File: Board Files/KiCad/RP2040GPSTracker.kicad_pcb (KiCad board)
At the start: 2 copper layers, 99.6 x 53 mm, 116 parts, among them J1 BOOTSEL, J10 GNSS, J2 RESET, J3 DEBUG, J4 BT(LE), J5 GSM, J6 USBC_CHARGE, J7 USBC_PROG, J8 2822541-1, J9 BATTERY, U1 W25Q128JVS, U10 LM66200DRLR, U2 SIM868, U3 RP2040, U4 SN74LVC1G66DRYR, U5 LM66200DRLR, U6 MP2624GL, U7 NCP1117LPST33T3G, U8 SAFFB1G56KB0F5F, Y1 Crystal

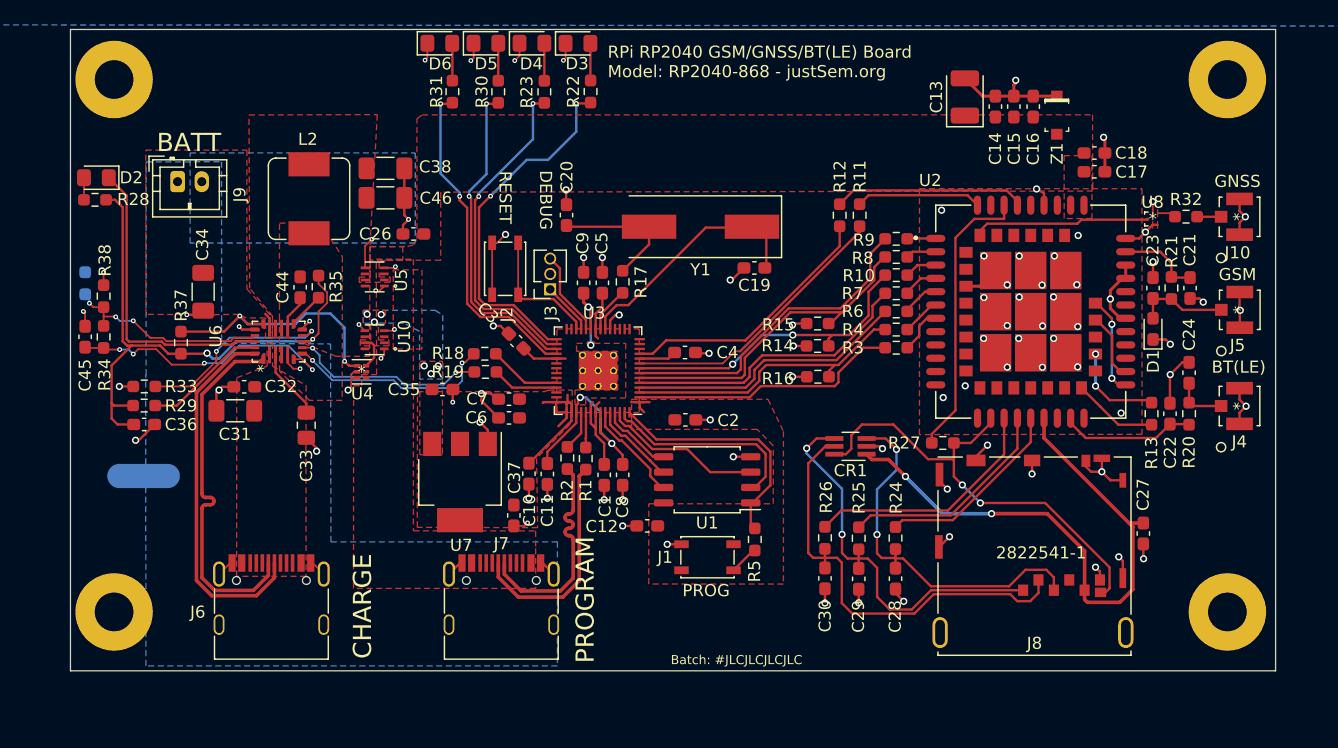
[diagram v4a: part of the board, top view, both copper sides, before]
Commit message: Rev 1.3. Implemented USB-C CC Channels. Fixed Z1 rotation. Expanded GPIO
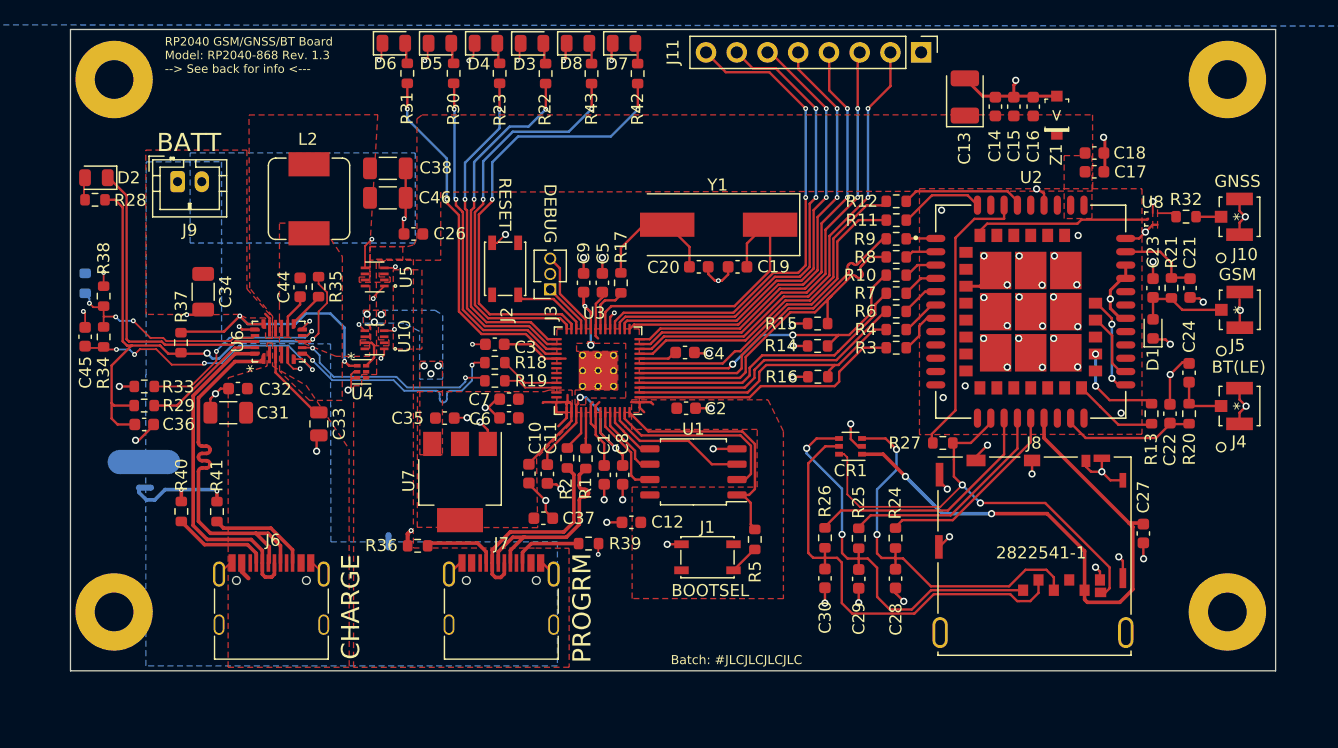
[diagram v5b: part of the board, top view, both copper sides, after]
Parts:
- removed REF**: Symbol_CC-Noncommercial_SilkscreenTop_Small, Symbol:Symbol_CC-Noncommercial_SilkscreenTop_Small
- removed REF**: Symbol_CC-Attribution_SilkscreenTop_Small, Symbol:Symbol_CC-Attribution_SilkscreenTop_Small
- removed REF**: Symbol_CC-ShareAlike_SilkscreenTop_Small, Symbol:Symbol_CC-ShareAlike_SilkscreenTop_Small
- removed REF**: Symbol_CreativeCommons_SilkscreenTop_Type2_Small, Symbol:Symbol_CreativeCommons_SilkscreenTop_Type2_Small
- added D7: LED, LED_SMD:LED_0805_2012Metric, F.Cu at (117.1, 5.01)
- added D8: LED, LED_SMD:LED_0805_2012Metric, F.Cu at (113.3, 5.01)
- added J11: GPIO9-15, Connector_PinHeader_2.54mm:PinHeader_1x08_P2.54mm_Vertical, F.Cu at (141.7, 5.76)
- added NT2: NetTie_2, NetTie:NetTie-2_SMD_Pad0.5mm, B.Cu at (77.6, 41.7)
- added NT3: NetTie_2, NetTie:NetTie-2_SMD_Pad0.5mm, B.Cu at (97.7, 46.2)
- added R36: 5.6k, Resistor_SMD:R_0603_1608Metric, F.Cu at (100.1, 46.5)
- added R39: 5.6k, Resistor_SMD:R_0603_1608Metric, F.Cu at (114.2, 46.3)
- added R40: 5.6k, Resistor_SMD:R_0603_1608Metric, F.Cu at (80.6, 43.7)
- added R41: 5.6k, Resistor_SMD:R_0603_1608Metric, F.Cu at (83.5, 43.7)
- added R42: 330, Resistor_SMD:R_0603_1608Metric, F.Cu at (118.3, 7.51)
- added R43: 330, Resistor_SMD:R_0603_1608Metric, F.Cu at (114.5, 7.51)
- C1, C10, C11, C12, C14, C15, C16, C17, C18, C19, C2, C20, C21, C22, C23, C24, C26, C27, C3, C32, C35, C36, C37, C4, C44, C45, C5, C6, C7, C8, C9: footprint Capacitor_SMD:C_0603_1608Metric_Pad1.08x0.95mm_HandSolder -> Capacitor_SMD:C_0603_1608Metric
- C28, C29, C30: value 100nF -> 22pF; footprint Capacitor_SMD:C_0603_1608Metric_Pad1.08x0.95mm_HandSolder -> Capacitor_SMD:C_0603_1608Metric
- C31, C34, C38, C46: footprint Capacitor_SMD:C_1206_3216Metric_Pad1.33x1.80mm_HandSolder -> Capacitor_SMD:C_1206_3216Metric
- C33: footprint Capacitor_SMD:C_0805_2012Metric_Pad1.18x1.45mm_HandSolder -> Capacitor_SMD:C_0805_2012Metric
- CR1: footprint Package_TO_SOT_SMD:SOT-363_SC-70-6_Handsoldering -> Package_TO_SOT_SMD:SOT-363_SC-70-6
- D1: footprint Diode_SMD:D_0603_1608Metric_Pad1.05x0.95mm_HandSolder -> Diode_SMD:D_0603_1608Metric
- D2, D3, D4, D5, D6: footprint LED_SMD:LED_0805_2012Metric_Pad1.15x1.40mm_HandSolder -> LED_SMD:LED_0805_2012Metric
- R1, R10, R11, R12, R13, R14, R15, R16, R17, R18, R19, R2, R20, R21, R22, R23, R24, R25, R26, R27, R28, R29, R3, R30, R31, R32, R33, R34, R35, R37, R38, R4, R5, R6, R7, R8, R9, TH1: footprint Resistor_SMD:R_0603_1608Metric_Pad0.98x0.95mm_HandSolder -> Resistor_SMD:R_0603_1608Metric
- moved C20 11.7 mm to (123.3, 23.5), turned to 0 degrees
- moved R12 4.81 mm to (139.6, 18.1), turned to 180 degrees
- moved R31 4.02 mm to (99.2, 7.49)
- moved R22 4.00 mm to (110.7, 7.51)
- moved R23 4.00 mm to (106.9, 7.49)
- moved R30 3.99 mm to (103.1, 7.49)
- moved D3 3.80 mm to (109.5, 5.01)
- moved D4 3.80 mm to (105.7, 5.00)
- moved D5 3.80 mm to (101.9, 5.00)
- moved D6 3.80 mm to (98.1, 5.00)
- moved R11 3.06 mm to (139.6, 19.6), turned to 180 degrees
- moved C37 2.45 mm to (110.5, 44.3), turned to 180 degrees
- moved C35 2.37 mm to (102.3, 36.0)
- moved C3 1.79 mm to (106.5, 29.9), turned to 0 degrees
- moved Y1 1.51 mm to (125.0, 20.0)
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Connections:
- J6 pad A5: unconnected-(J6-PadA5) -> Net-(J6-PadA5)
- J6 pad B5: unconnected-(J6-PadB5) -> Net-(J6-PadB5)
- J6 pad B6: unconnected-(J6-PadB6) -> /BCM_D+
- J6 pad B7: unconnected-(J6-PadB7) -> /BCM_D-
- J7 pad A5: unconnected-(J7-PadA5) -> Net-(J7-PadA5)
- J7 pad B5: unconnected-(J7-PadB5) -> Net-(J7-PadB5)
- J7 pad B6: unconnected-(J7-PadB6) -> /USB_D+
- J7 pad B7: unconnected-(J7-PadB7) -> /USB_D-
- U2 pad 41: (no net) -> unconnected-(U2-Pad41)
- U3 pad 12: unconnected-(U3-Pad12) -> /IO_1
- U3 pad 13: unconnected-(U3-Pad13) -> /IO_2
- U3 pad 14: unconnected-(U3-Pad14) -> /IO_3
- U3 pad 15: unconnected-(U3-Pad15) -> /IO_4
- U3 pad 16: unconnected-(U3-Pad16) -> /IO_5
- U3 pad 17: unconnected-(U3-Pad17) -> /IO_6
- U3 pad 18: unconnected-(U3-Pad18) -> /IO_7
- U3 pad 27: unconnected-(U3-Pad27) -> Net-(U3-Pad27)
- U3 pad 28: unconnected-(U3-Pad28) -> Net-(U3-Pad28)
- Z1 pad A: /SIM_PWR -> GND
- Z1 pad K: GND -> /SIM_PWR
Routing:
- net /IO_7: track 0.00 -> 41.4 mm, vias 0 -> 2
- net /IO_6: track 0.00 -> 39.9 mm, vias 0 -> 2
- net /IO_1: track 0.00 -> 38.7 mm, vias 0 -> 2
- net /IO_5: track 0.00 -> 38.4 mm, vias 0 -> 2
- net /IO_4: track 0.00 -> 37.6 mm, vias 0 -> 2
- net /IO_2: track 0.00 -> 37.2 mm, vias 0 -> 2
- net /IO_3: track 0.00 -> 37.0 mm, vias 0 -> 2
- net Net-(U3-Pad27): track 0.00 -> 36.9 mm, vias 0 -> 2
- net Net-(U3-Pad28): track 0.00 -> 33.6 mm, vias 0 -> 2
- net GND: track 125.2 -> 137.1 mm, vias 88 -> 92
- net Net-(J6-PadB5): track 0.00 -> 8.30 mm
- net Net-(J6-PadA5): track 0.00 -> 8.08 mm
- net Net-(J7-PadA5): track 0.00 -> 6.16 mm
- net Net-(J7-PadB5): track 0.00 -> 5.72 mm
- net /SIM_PWRKEY: track 15.9 -> 10.2 mm
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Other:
- board text added: "10"
- board text added: "11"
- board text added: "12"
- board text added: "13"
- board text added: "14"
- board text added: "15"
- board text added: "16"
- board text added: "17"
- board text added: "18"
- board text added: "19"
- board text added: "20"
- board text added: "21"
- board text added: "9"
- board text added: ">"
- board text added: "BOOTSEL"
- board text added: "Board Rev.: 1.3 18-03-2022"
- board text added: "GND"
- board text added: "GPIO#:"
- board text added: "Get started at wiki.justsem.org/rp2040-868"
- board text added: "LED D3"
- board text added: "LED D4"
- board text added: "LED D5"
- board text added: "LED D6"
- board text added: "LED D7"
- board text added: "LED D8"
- board text added: "PROGRM"
- board text added: "RP2040 GSM/GNSS/BT Board Model: RP2040-868 Rev. 1.3 --> See back for info <---"
- board text removed: "Board Rev.: 1.2 16-03-2022"
- board text removed: "Get started at docs.justsem.org/rp2040-868"
- board text removed: "PROG"
- board text removed: "PROGRAM"
- board text removed: "RPi RP2040 GSM/GNSS/BT(LE) Board Model: RP2040-868 - justSem.org"

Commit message: Rev 2.0
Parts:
- added ?: , RP2040-868Graphics:charge-fs, F.Cu at (94.4, 55.5)
- added ?: , RP2040-868Graphics:bt-re, F.Cu at (166.2, 32.0)
- added ?: , RP2040-868Graphics:gnss-re, F.Cu at (165.2, 16.3)
- added ?: , RP2040-868Graphics:program-fs, F.Cu at (113.6, 56.2)
- added ?: , RP2040-868Graphics:batt-ca, F.Cu at (81.6, 18.1)
- added ?: , RP2040-868Graphics:debug-ha, F.Cu at (114.3, 12.0)
- added ?: , RP2040-868Graphics:r2_0-ca, B.Cu at (136.1, 53.4)
- added ?: , RP2040-868Graphics:date-cc-ha, B.Cu at (141.9, 55.1)
- added ?: , RP2040-868Graphics:rev-cc-ha, B.Cu at (141.9, 53.4)
- added ?: , RP2040-868Graphics:9-ca, B.Cu at (139.2, 9.81)
- added ?: , RP2040-868Graphics:14-ca, B.Cu at (126.4, 10.5)
- added ?: , RP2040-868Graphics:status-lc-ha-left, F.Cu at (75.4, 14.7)
- added ?: , RP2040-868Graphics:12-ca, B.Cu at (131.5, 10.5)
- added ?: , RP2040-868Graphics:wikiref-re, B.Cu at (126.7, 28.2)
- added ?: , RP2040-868Graphics:15-ca, B.Cu at (123.9, 10.4)
- added ?: , RP2040-868Graphics:3v3-lc-ca, B.Cu at (121.4, 11.8)
- added ?: , RP2040-868Graphics:gnd-ca, B.Cu at (141.7, 12.1)
- added ?: , RP2040-868Graphics:13-ca, B.Cu at (129.0, 10.5)
- added ?: , RP2040-868Graphics:11-ca, B.Cu at (134.1, 10.3)
- added ?: , RP2040-868Graphics:10-ca, B.Cu at (136.6, 10.5)
- added ?: , RP2040-868Graphics:status-lc-ha, F.Cu at (82.2, 4.99)
- added ?: , RP2040-868Graphics:gsm-re, F.Cu at (165.5, 24.1)
- added ?: , RP2040-868Graphics:gpio-ca, F.Cu at (129.2, 8.38)
- added ?: , RP2040-868Graphics:boot-ca, F.Cu at (117.9, 48.6)
- added ?: , RP2040-868Graphics:reset-ca, F.Cu at (107.6, 21.1)
- added ?: , RP2040-868Graphics:rp2040-868-re, F.Cu at (128.1, 51.8)
- added ?: , RP2040-868Graphics:jsorg-fs, F.Cu at (128.2, 50.1)
- added D10: BLUE, LED_SMD:LED_0805_2012Metric, F.Cu at (90.5, 5.00)
- added D11: BLUE, LED_SMD:LED_0805_2012Metric, F.Cu at (155.5, 11.5)
- added D9: BLUE, LED_SMD:LED_0805_2012Metric, F.Cu at (94.3, 5.00)
- added Q1: Si2319CDS, Package_TO_SOT_SMD:SOT-23, F.Cu at (104.3, 27.1)
- added Q2: Si2319CDS, Package_TO_SOT_SMD:SOT-23, F.Cu at (159.9, 11.7)
- added R44: 20, Resistor_SMD:R_0603_1608Metric, F.Cu at (95.3, 7.49)
- added R45: 100, Resistor_SMD:R_0603_1608Metric, F.Cu at (91.5, 7.49)
- added R46: 47k, Resistor_SMD:R_0603_1608Metric, F.Cu at (159.1, 14.7)
- added R47: 4.7k, Resistor_SMD:R_0603_1608Metric, F.Cu at (159.1, 16.3)
- added R48: 56, Resistor_SMD:R_0603_1608Metric, F.Cu at (157.3, 11.3)
- added R49: DNF, Resistor_SMD:R_0402_1005Metric, F.Cu at (123.1, 36.5)
- added REF**: Symbol_CC-Attribution_SilkscreenTop_Small, Symbol:Symbol_CC-Attribution_SilkscreenTop_Small, B.Cu at (127.0, 39.6)
- added REF**: Symbol_CreativeCommons_SilkscreenTop_Type2_Small, Symbol:Symbol_CreativeCommons_SilkscreenTop_Type2_Small, B.Cu at (142.0, 39.6)
- added REF**: Symbol_CC-Noncommercial_SilkscreenTop_Small, Symbol:Symbol_CC-Noncommercial_SilkscreenTop_Small, B.Cu at (97.0, 39.6)
- added REF**: Symbol_CC-ShareAlike_SilkscreenTop_Small, Symbol:Symbol_CC-ShareAlike_SilkscreenTop_Small, B.Cu at (112.0, 39.6)
- added TP1: TestPoint, TestPoint:TestPoint_Pad_1.5x1.5mm, B.Cu at (105.5, 54.5)
- added TP2: TestPoint, TestPoint:TestPoint_Pad_1.5x1.5mm, B.Cu at (108.5, 54.5)
- added TP3: TestPoint, TestPoint:TestPoint_Pad_1.5x1.5mm, B.Cu at (117.0, 39.0)
- added TP4: TestPoint, TestPoint:TestPoint_Pad_1.5x1.5mm, B.Cu at (101.3, 40.1)
- added TP5: TestPoint, TestPoint:TestPoint_Pad_1.5x1.5mm, B.Cu at (155.8, 11.0)
- added TP6: TestPoint, TestPoint:TestPoint_Pad_1.5x1.5mm, B.Cu at (109.9, 19.2)
- added TP7: TestPoint, TestPoint:TestPoint_Pad_1.5x1.5mm, B.Cu at (120.8, 48.1)
- added TP8: TestPoint, TestPoint:TestPoint_Pad_1.5x1.5mm, B.Cu at (88.0, 12.3)
- added TP9: TestPoint, TestPoint:TestPoint_Pad_1.5x1.5mm, B.Cu at (78.9, 25.9)
- C1, C10, C11, C12, C2, C3, C4, C5, C6, C7, C8, C9: footprint Capacitor_SMD:C_0603_1608Metric -> Capacitor_SMD:C_0402_1005Metric
- C27, C28, C29, C30, R24, R25, R26, R27: moved to B.Cu
- D3, D7, D8: value LED -> RED
- D4, D5, D6: value LED -> BLUE
- J1, J2: footprint Button_Switch_SMD:TS-1145A-C-A -> Button_Switch_SMD:SW_SPST_ALPS_SKRKAEE020
- J11: footprint Connector_PinHeader_2.54mm:PinHeader_1x08_P2.54mm_Vertical -> Connector_PinHeader_2.54mm:PinHeader_1x09_P2.54mm_Vertical
- J9: footprint Connector_JST:JST_PH_B2B-PH-K_1x02_P2.00mm_Vertical -> Connector_JST:JST_PH_S2B-PH-K_1x02_P2.00mm_Horizontal
- R22, R42, R43: value 330 -> 56
- R23, R30, R31: value 330 -> 20
- R28: value 1k -> 100/0.2
- R36, R39, R40, R41: value 5.6k -> 5.1k; footprint Resistor_SMD:R_0603_1608Metric -> Resistor_SMD:R_0402_1005Metric
- U1: footprint Package_SO:SOIC-8_5.23x5.23mm_P1.27mm -> Package_SON:WSON-8-1EP_6x5mm_P1.27mm_EP3.4x4.3mm
- Y1: footprint Crystal:Crystal_SMD_HC49-SD -> ABRACON:ABMM2-12.000MHZ-E2-T
- moved CR1 27.3 mm to (160.8, 49.2), turned to -90 degrees
- moved C30 17.9 mm to (151.3, 52.4)
- moved R26 17.5 mm to (151.3, 46.3)
- moved R27 15.5 mm to (156.6, 46.2), turned to -90 degrees
- moved C28 13.7 mm to (152.9, 52.4)
- moved C29 13.6 mm to (149.8, 52.4)
- moved R24 13.2 mm to (152.8, 46.3)
- moved R25 13.2 mm to (149.7, 46.3)
- moved C27 8.61 mm to (155.2, 52.6)
- moved R15 7.62 mm to (139.5, 23.9), turned to 180 degrees
- moved C12 7.37 mm to (125.0, 43.2), turned to 0 degrees
- moved R14 7.03 mm to (139.5, 27.0), turned to 180 degrees
- moved C20 6.51 mm to (118.5, 19.1), turned to 90 degrees
- moved J3 6.50 mm to (114.3, 19.7), turned to 0 degrees
- moved R16 6.40 mm to (139.5, 31.6), turned to 180 degrees
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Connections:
- net Net-(J2-Pad1) renamed /PI_RESET
- net Net-(R1-Pad2) renamed /PI_D+
- net Net-(R2-Pad2) renamed /PI_D-
- net Net-(R22-Pad2) renamed /LED_3
- net Net-(R23-Pad2) renamed /LED_4
- net Net-(R30-Pad2) renamed /LED_5
- net Net-(R31-Pad2) renamed /LED_6
- net Net-(R5-Pad1) renamed /SPI_SS
- net Net-(U1-Pad2) renamed /SPI_IO1
- net Net-(U1-Pad3) renamed /SPI_IO2
- net Net-(U1-Pad5) renamed /SPI_IO0
- net Net-(U1-Pad6) renamed /SPI_CLK
- net Net-(U1-Pad7) renamed /SPI_IO3
- net Net-(U3-Pad27) renamed /LED_1
- net Net-(U3-Pad28) renamed /LED_2
- C20 pad 1: Net-(C20-Pad1) -> Net-(Y1-Pad3)
- CR1 pad 1: /SIM_C_VDD -> Net-(C30-Pad2)
- CR1 pad 3: Net-(C28-Pad2) -> /SIM_C_VDD
- CR1 pad 4: Net-(C29-Pad2) -> /SIM_C_DET
- CR1 pad 5: Net-(C30-Pad2) -> Net-(C28-Pad2)
- CR1 pad 6: /SIM_C_DET -> Net-(C29-Pad2)
- R17 pad 2: Net-(C20-Pad1) -> Net-(Y1-Pad3)
- U2 pad 41: unconnected-(U2-Pad41) -> /SIM_NETLIGHT
- U3 pad 36: unconnected-(U3-Pad36) -> /LED_7
- U3 pad 37: unconnected-(U3-Pad37) -> /LED_PWR
- Y1 pad 2: Net-(C20-Pad1) -> GND
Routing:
- net /LED_7: track 0.00 -> 33.5 mm, vias 0 -> 4
- net Net-(Q1-Pad3): track 0.00 -> 28.4 mm, vias 0 -> 2
- net /SIM_C_VDD: track 48.6 -> 24.6 mm
- net +3V3: track 37.4 -> 58.6 mm, vias 0 -> 3
- net Net-(C30-Pad2): track 37.4 -> 16.3 mm, vias 0 -> 1
- net /SIM_NETLIGHT: track 0.00 -> 17.5 mm, vias 0 -> 2
- net GND: track 137.1 -> 120.2 mm, vias 92 -> 90
- net Net-(C28-Pad2): track 31.7 -> 14.8 mm, vias 2 -> 1
- net Net-(C29-Pad2): track 33.4 -> 18.2 mm, vias 2 -> 1
- net /SIM_C_DET: track 40.7 -> 25.9 mm
- net /SIM_VDD_EXT: track 23.6 -> 37.4 mm, vias 0 -> 1
- net Net-(U3-Pad20): track 24.7 -> 11.9 mm
- net /LED_PWR: track 0.00 -> 11.3 mm
- net Net-(C20-Pad1): track 10.9 -> 0.00 mm
- net /SPI_IO1: track 15.6 -> 5.38 mm
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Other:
- outline, holes or cut-outs redrawn
- board text added: "+1.1V"
- board text added: "+3.3V"
- board text added: "+4V"
- board text added: "+5V"
- board text added: "24"
- board text added: "25"
- board text added: "26-03-2022"
- board text added: "800mA max!"
- board text added: "BOOT"
- board text added: "D+ D-"
- board text added: "Get started at"
- board text added: "LED D10"
- board text added: "LED D9"
- board text added: "PGND"
- board text added: "RUN"
- board text added: "STATUS"
- board text removed: "10"
- board text removed: "11"
- board text removed: "12"
- board text removed: "13"
- board text removed: "14"
- board text removed: "15"
- board text removed: "9"
- board text removed: "BATT"
- board text removed: "BOOTSEL"
- board text removed: "Board Rev.: 1.3 18-03-2022"
- board text removed: "CHARGE"
- board text removed: "DEBUG"
- board text removed: "GND"
- board text removed: "GPIO#:"
- board text removed: "Get started at wiki.justsem.org/rp2040-868"
- board text removed: "PROGRM"
- board text removed: "RESET"
- board text removed: "RP2040 GSM/GNSS/BT Board Model: RP2040-868 Rev. 1.3 --> See back for info <---"

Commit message: Rev 3.1 - Power-stage overhaul, SIM power finetuning
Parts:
- removed C26: 10uF, Capacitor_SMD:C_0603_1608Metric
- removed U5: LM66200DRLR, LM66200:LM66200DRLR
- removed U7: NCP1117LPST33T3G, Package_TO_SOT_SMD:SOT-223
- added C25: 22pF, Capacitor_SMD:C_0603_1608Metric, F.Cu at (101.9, 40.9)
- added G***: LOGO, QR:QR, F.Cu at (132.7, 42.2)
- added L1: 1uH, Inductor_SMD:L_1008_2520Metric, F.Cu at (105.9, 35.2)
- added R50: 100k, Resistor_SMD:R_0603_1608Metric, F.Cu at (104.9, 42.4)
- added R51: 22k, Resistor_SMD:R_0603_1608Metric, F.Cu at (101.8, 42.4)
- U4: value SN74LVC1G66DRYR -> RT8096; footprint TI_LV74XXG6:SN74LVC1G66DRYR -> Package_TO_SOT_SMD:TSOT-23-5
- Y1: footprint ABRACON:ABMM2-12.000MHZ-E2-T -> Crystal:Crystal_SMD_HC49-SD
- moved ? 22.1 mm to (72.5, 36.6), turned to -90 degrees
- moved D2 19.2 mm to (73.5, 33.9)
- moved R28 19.2 mm to (73.2, 35.6)
- moved U4 9.34 mm to (102.4, 38.4), turned to 180 degrees
- moved TP4 6.60 mm to (107.7, 41.9)
- moved Q1 5.64 mm to (104.4, 21.5)
- moved R17 3.66 mm to (118.1, 25.8), turned to 0 degrees
- moved C19 3.16 mm to (127.1, 25.8), turned to 180 degrees
- moved U10 2.78 mm to (95.2, 32.0), turned to 90 degrees
- moved C37 2.17 mm to (109.1, 38.2), turned to -90 degrees
- moved Y1 1.97 mm to (123.4, 22.4)
- moved C35 1.34 mm to (102.4, 35.8)
- moved ? 1.13 mm to (127.3, 50.9)
- moved ? 1.13 mm to (127.4, 49.3)
- moved C20 1.05 mm to (119.5, 19.0), turned to 0 degrees
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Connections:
- C13 pad 1: /SIM_PWR -> /BOOST_OUT
- C14 pad 1: /SIM_PWR -> /BOOST_OUT
- C15 pad 1: /SIM_PWR -> /BOOST_OUT
- C16 pad 1: /SIM_PWR -> /BOOST_OUT
- C17 pad 1: /SIM_PWR -> /BOOST_OUT
- C18 pad 2: /SIM_PWR -> /BOOST_OUT
- C20 pad 1: Net-(Y1-Pad3) -> Net-(C20-Pad1)
- C37 pad 1: GND -> +3V3
- C37 pad 2: +3V3 -> GND
- D11 pad 2: /SIM_PWR -> /BOOST_OUT
- R17 pad 2: Net-(Y1-Pad3) -> Net-(C20-Pad1)
- U2 pad 34: /SIM_PWR -> /BOOST_OUT
- U2 pad 35: /SIM_PWR -> /BOOST_OUT
- U4 pad 1: /BCM_DISC -> /PI_VREG_IN
- U4 pad 3: GND -> /PI_VREG_SW
- U4 pad 4: /PROG_VBUS -> /PI_VREG_IN
- U4 pad 5: unconnected-(U4-Pad5) -> /PI_VREG_FB
- Y1 pad 2: GND -> Net-(C20-Pad1)
- Z1 pad K: /SIM_PWR -> /BOOST_OUT
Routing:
- net +3V3: track 58.6 -> 80.7 mm
- net /BCM_VREF_1: track 47.7 -> 30.1 mm
- net /BCM_DISC: track 20.6 -> 7.07 mm, vias 2 -> 0
- net Net-(D2-Pad1): track 26.4 -> 14.9 mm
- net GND: track 120.2 -> 110.7 mm, vias 90 -> 87
- net Net-(C20-Pad1): track 0.00 -> 7.15 mm
- net Net-(Q1-Pad3): track 28.4 -> 21.5 mm
- net /IO_7: track 34.7 -> 41.1 mm
- net Net-(C19-Pad1): track 11.9 -> 18.2 mm
- net /PI_VREG_FB: track 0.00 -> 6.22 mm
- net /IO_6: track 34.3 -> 39.9 mm
- net /IO_5: track 33.7 -> 39.0 mm
- net /IO_4: track 34.0 -> 38.4 mm
- net /LED_PWR: track 11.3 -> 15.6 mm
- net Net-(Y1-Pad3): track 4.14 -> 0.00 mm
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- added copper zone on F.Cu, net /PI_VREG_SW
- removed copper zone on B.Cu, net /PI_VREG_IN
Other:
- board text added: "To power SIM Connect BATT or CHARGE"
